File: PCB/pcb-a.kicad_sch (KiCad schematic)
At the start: 16 parts, among them Q3 BC337, Q4 BC337, SW1 config, U1 MCP23008-xP, U4 ATmega16L-8P

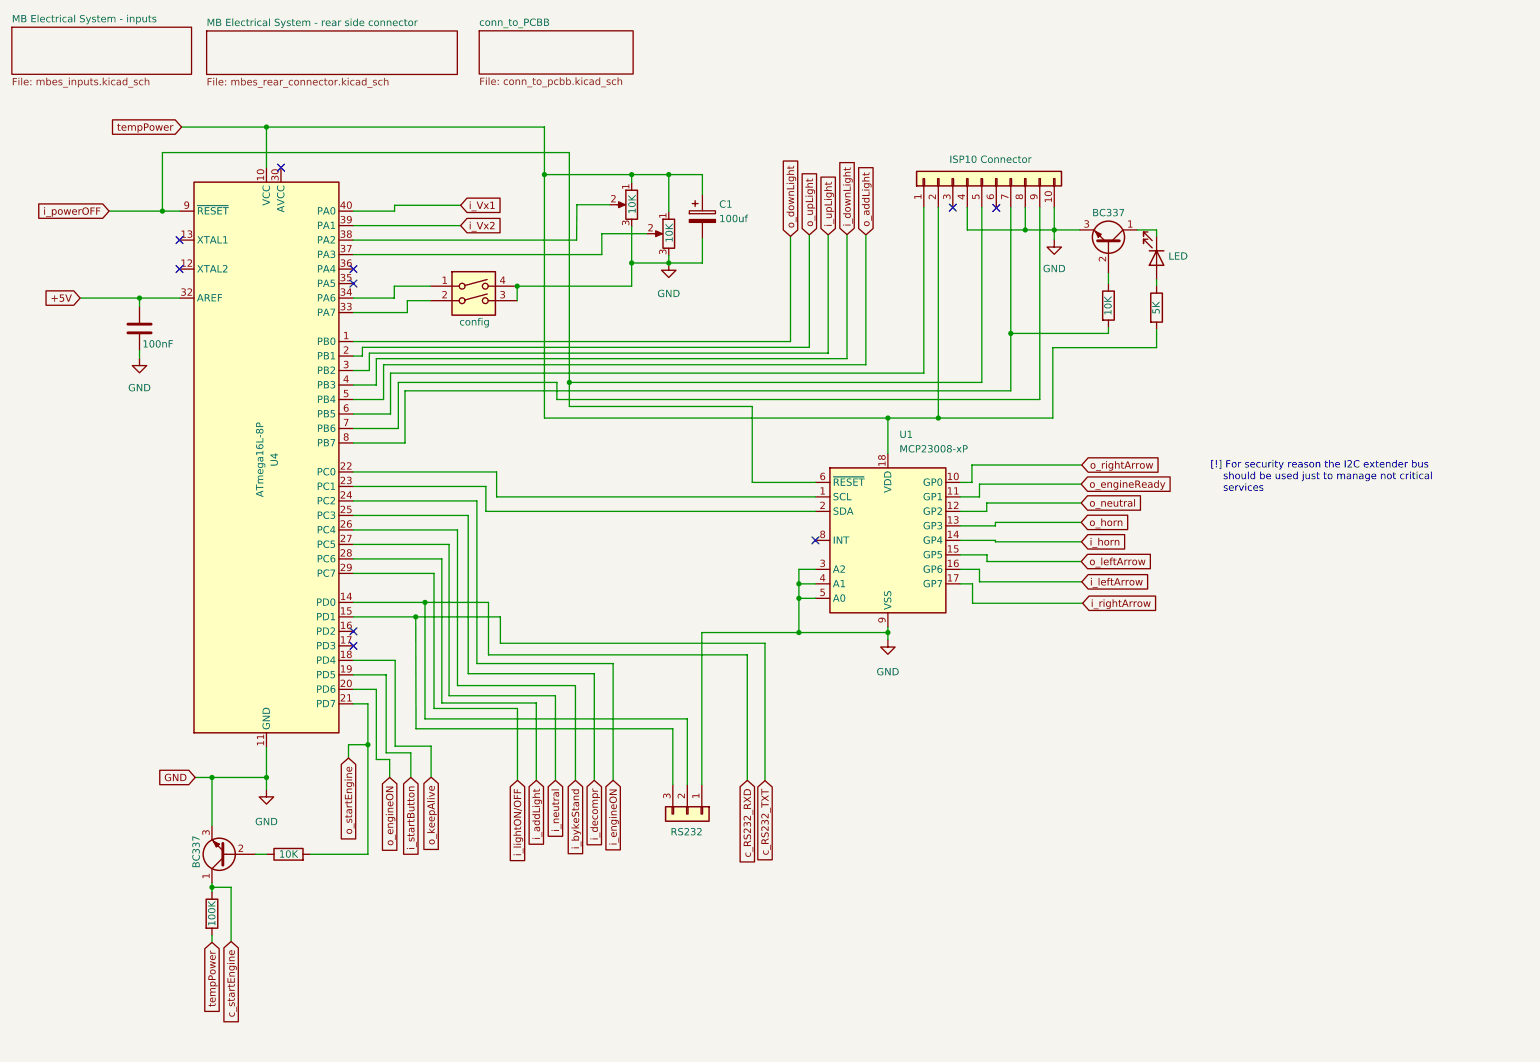
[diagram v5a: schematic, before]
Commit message: Fix: RESET pin and RS232 port fingerprint
- pull-up  resistor added to RESET pin
- RS232 port fingerprint resized to standard 4-pin port
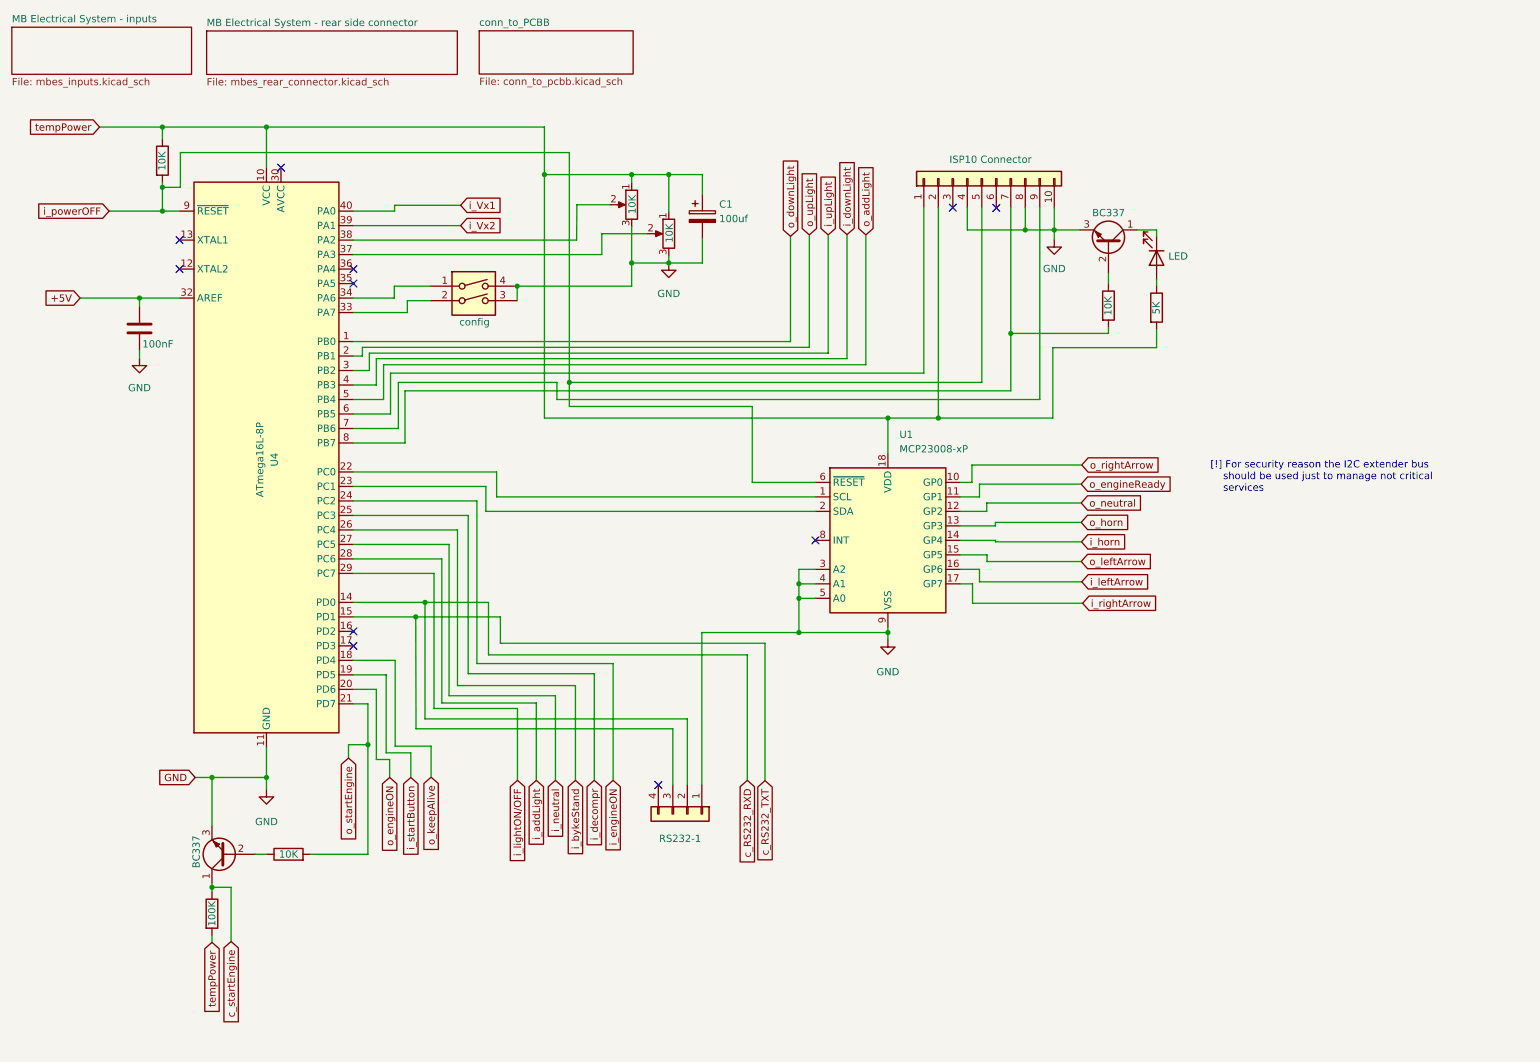
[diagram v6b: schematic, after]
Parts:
- removed RS232-1: RS232, Connector_PinSocket_2.54mm:PinSocket_1x03_P2.54mm_Vertical, symbol Connector_Generic:Conn_01x03
- added R2: 10K, Resistor_THT:R_Axial_DIN0207_L6.3mm_D2.5mm_P7.62mm_Horizontal, symbol Device:R
- added RS232-1: Conn_01x04, Connector_PinHeader_2.54mm:PinHeader_1x04_P2.54mm_Vertical, symbol Connector_Generic:Conn_01x04
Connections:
- net GND: now also RS232-1.1 (Pin_1)
- net c_RS232_RXD: now also RS232-1.2 (Pin_2)
- net c_RS232_TXT: now also RS232-1.3 (Pin_3)
- net i_powerOFF: now also R2.2
- net tempPower: now also R2.1
- no-connect marks 10 -> 11
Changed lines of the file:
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@@
   (junction (at 59.0804 149.3012) (diameter 0) (color 0 0 0 0)
   )
+  (junction (at 40.8432 35.306) (diameter 0) (color 0 0 0 0)
+  )
   (junction (at 103.0224 63.1952) (diameter 0) (color 0 0 0 0)
   )
@@
   )
   (junction (at 107.7976 43.6372) (diameter 0) (color 0 0 0 0)
+  )
+  (junction (at 40.8432 45.8724) (diameter 0) (color 0 0 0 0)
   )
   (junction (at 86.868 118.618) (diameter 0) (color 0 0 0 0)
@@
   (no_connect (at 74.3204 62.738))
   (no_connect (at 186.9948 49.4792))
+  (no_connect (at 127.762 150.622))
   (no_connect (at 61.6204 42.418))
   (no_connect (at 74.3204 60.198))
@@
     (stroke (width 0) (type default) (color 0 0 0 0))
   )
+  (wire (pts (xy 43.9928 39.7764) (xy 112.1664 39.7764))
+    (stroke (width 0) (type default) (color 0 0 0 0))
+  )
   (wire (pts (xy 123.0884 59.1312) (xy 123.0884 52.7304))
     (stroke (width 0) (type default) (color 0 0 0 0))
@@
     (stroke (width 0) (type default) (color 0 0 0 0))
   )
+  (wire (pts (xy 40.8432 45.8724) (xy 43.9928 45.8724))
+    (stroke (width 0) (type default) (color 0 0 0 0))
+  )
   (wire (pts (xy 74.3204 67.818) (xy 83.7692 67.818))
     (stroke (width 0) (type default) (color 0 0 0 0))
@@
     (stroke (width 0) (type default) (color 0 0 0 0))
   )
-  (wire (pts (xy 40.8432 39.7764) (xy 112.1664 39.7764))
-    (stroke (width 0) (type default) (color 0 0 0 0))
-  )
   (wire (pts (xy 135.4836 43.6372) (xy 129.5908 43.6372))
     (stroke (width 0) (type default) (color 0 0 0 0))
@@
     (stroke (width 0) (type default) (color 0 0 0 0))
   )
-  (wire (pts (xy 40.8432 50.038) (xy 40.8432 39.7764))
+  (wire (pts (xy 40.8432 50.038) (xy 40.8432 45.8724))
     (stroke (width 0) (type default) (color 0 0 0 0))
   )
@@
     (stroke (width 0) (type default) (color 0 0 0 0))
   )
+  (wire (pts (xy 43.9928 45.8724) (xy 43.9928 39.7764))
+    (stroke (width 0) (type default) (color 0 0 0 0))
+  )
   (wire (pts (xy 79.6036 83.058) (xy 79.6036 76.962))
     (stroke (width 0) (type default) (color 0 0 0 0))
@@
     (stroke (width 0) (type default) (color 0 0 0 0))
   )
+  (wire (pts (xy 40.8432 35.306) (xy 40.8432 37.3888))
+    (stroke (width 0) (type default) (color 0 0 0 0))
+  )
   (wire (pts (xy 74.3204 77.978) (xy 77.1144 77.978))
     (stroke (width 0) (type default) (color 0 0 0 0))
@@
     (stroke (width 0) (type default) (color 0 0 0 0))
   )
+  (wire (pts (xy 40.8432 45.8724) (xy 40.8432 45.0088))
+    (stroke (width 0) (type default) (color 0 0 0 0))
+  )
   (wire (pts (xy 185.3184 102.6668) (xy 180.6956 102.6668))
     (stroke (width 0) (type default) (color 0 0 0 0))
   )
-  (wire (pts (xy 44.196 35.306) (xy 59.0804 35.306))
+  (wire (pts (xy 29.8196 35.306) (xy 40.8432 35.306))
     (stroke (width 0) (type default) (color 0 0 0 0))
   )
@@
   )
   (wire (pts (xy 91.0844 134.9756) (xy 91.0844 108.458))
+    (stroke (width 0) (type default) (color 0 0 0 0))
+  )
+  (wire (pts (xy 40.8432 35.306) (xy 59.0804 35.306))
     (stroke (width 0) (type default) (color 0 0 0 0))
   )
@@
     )
   )
-  (global_label "tempPower" (shape input) (at 44.196 35.306 180) (fields_autoplaced)
-    (effects (font (size 1.27 1.27)) (justify right))
-    (property "Riferimenti inter-foglio" "${INTERSHEET_REFS}" (id 0) (at 31.5019 35.3854 0)
+  (global_label "tempPower" (shape input) (at 29.8196 35.306 180) (fields_autoplaced)
+    (effects (font (size 1.27 1.27)) (justify right))
+    (property "Riferimenti inter-foglio" "${INTERSHEET_REFS}" (id 0) (at 17.1255 35.3854 0)
       (effects (font (size 1.27 1.27)) (justify right) hide)
     )
@@
     (pin "9")
   )
+  (symbol (lib_id "Device:R") (at 40.8432 41.1988 0) (unit 1)
+    (in_bom yes) (on_board yes)
+    (property "Reference" "R2" (id 0) (at 46.482 41.1988 90)
+      (effects (font (size 1.27 1.27)) hide)
+    )
+    (property "Value" "10K" (id 1) (at 40.7924 41.2496 90))
+    (property "Footprint" "Resistor_THT:R_Axial_DIN0207_L6.3mm_D2.5mm_P7.62mm_Horizontal" (id 2) (at 39.0652 41.1988 90)
+      (effects (font (size 1.27 1.27)) hide)
+    )
+    (property "Datasheet" "~" (id 3) (at 40.8432 41.1988 0)
+      (effects (font (size 1.27 1.27)) hide)
+    )
+    (pin "1")
+    (pin "2")
+  )
   (symbol (lib_id "power:GND") (at 197.1548 55.0672 0) (unit 1)
     (in_bom yes) (on_board yes) (fields_autoplaced)
@@
     (pin "3")
     (pin "4")
-  )
-  (symbol (lib_id "Connector_Generic:Conn_01x03") (at 132.842 155.702 270) (unit 1)
-    (in_bom yes) (on_board yes)
-    (property "Reference" "RS232-1" (id 0) (at 128.7272 158.8516 90)
-      (effects (font (size 1.27 1.27)) (justify left) hide)
-    )
-    (property "Value" "RS232" (id 1) (at 129.8956 158.8516 90)
-      (effects (font (size 1.27 1.27)) (justify left))
-    )
-    (property "Footprint" "Connector_PinSocket_2.54mm:PinSocket_1x03_P2.54mm_Vertical" (id 2) (at 132.842 155.702 0)
-      (effects (font (size 1.27 1.27)) hide)
-    )
-    (property "Datasheet" "~" (id 3) (at 132.842 155.702 0)
-      (effects (font (size 1.27 1.27)) hide)
-    )
-    (pin "1")
-    (pin "2")
-    (pin "3")
   )
   (symbol (lib_id "Device:R") (at 206.6544 66.5988 0) (unit 1)
@@
     (pin "2")
     (pin "3")
+  )
+  (symbol (lib_id "Connector_Generic:Conn_01x04") (at 132.842 155.702 270) (unit 1)
+    (in_bom yes) (on_board yes) (fields_autoplaced)
+    (property "Reference" "RS232-1" (id 0) (at 131.572 160.02 90))
+    (property "Value" "Conn_01x04" (id 1) (at 131.572 162.56 90)
+      (effects (font (size 1.27 1.27)) hide)
+    )
+    (property "Footprint" "Connector_PinHeader_2.54mm:PinHeader_1x04_P2.54mm_Vertical" (id 2) (at 132.842 155.702 0)
+      (effects (font (size 1.27 1.27)) hide)
+    )
+    (property "Datasheet" "~" (id 3) (at 132.842 155.702 0)
+      (effects (font (size 1.27 1.27)) hide)
+    )
+    (pin "1")
+    (pin "2")
+    (pin "3")
+    (pin "4")
   )
   (symbol (lib_id "power:GND") (at 36.83 75.8444 0) (unit 1)
@@
       (reference "R1") (unit 1) (value "1K") (footprint "Resistor_THT:R_Axial_DIN0207_L6.3mm_D2.5mm_P7.62mm_Horizontal")
     )
+    (path "/720930cf-ec82-4dc2-994a-09298296c03d"
+      (reference "R2") (unit 1) (value "10K") (footprint "Resistor_THT:R_Axial_DIN0207_L6.3mm_D2.5mm_P7.62mm_Horizontal")
+    )
     (path "/b1e0026b-e442-4e9d-9275-b07005f83053"
       (reference "R6") (unit 1) (value "100K") (footprint "Resistor_THT:R_Axial_DIN0207_L6.3mm_D2.5mm_P7.62mm_Horizontal")
@@
       (reference "R9") (unit 1) (value "5K") (footprint "Resistor_THT:R_Axial_DIN0207_L6.3mm_D2.5mm_P7.62mm_Horizontal")
     )
-    (path "/9642f9cf-4b46-422a-a864-ecd9c3909353"
-      (reference "RS232-1") (unit 1) (value "RS232") (footprint "Connector_PinSocket_2.54mm:PinSocket_1x03_P2.54mm_Vertical")
+    (path "/c9774949-c461-4c76-91ad-3c30a5da3235"
+      (reference "RS232-1") (unit 1) (value "Conn_01x04") (footprint "Connector_PinHeader_2.54mm:PinHeader_1x04_P2.54mm_Vertical")
     )
     (path "/dfeffa1f-9119-4780-8aed-ab76c9242c17"

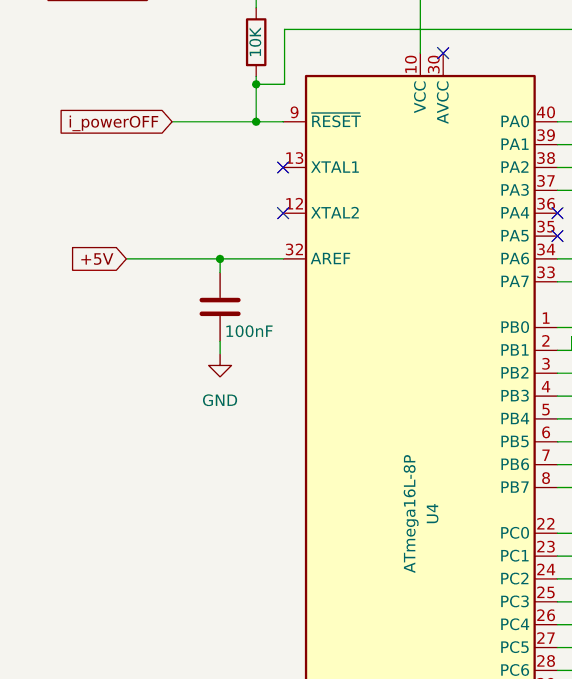
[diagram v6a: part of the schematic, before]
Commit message: External oscillator
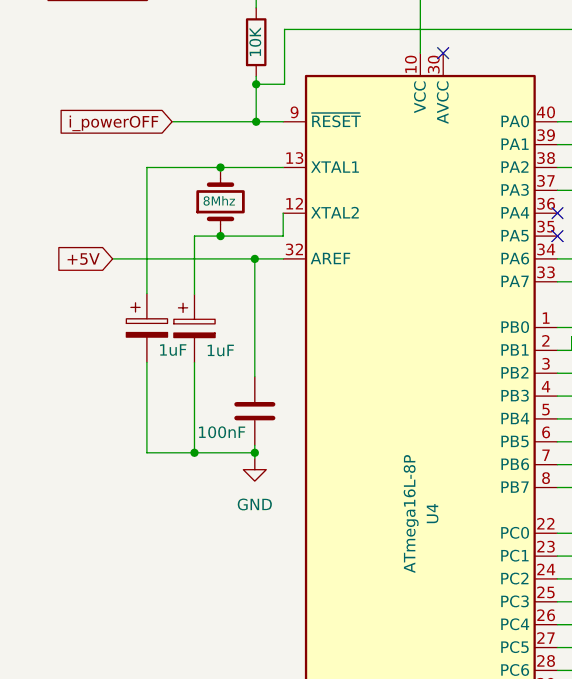
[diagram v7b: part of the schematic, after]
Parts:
- added C3, C4: 1uF, Capacitor_THT:CP_Radial_D6.3mm_P2.50mm, symbol Device:C_Polarized
- added Y1: 8Mhz, Crystal:Crystal_HC49-U_Vertical, symbol Device:Crystal
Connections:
- net GND: now also C3.2, C4.2
- net at U4.12 (XTAL2): now also C4.1, Y1.1
- net at U4.13 (XTAL1): now also C3.1, Y1.2
- no-connect marks 11 -> 9

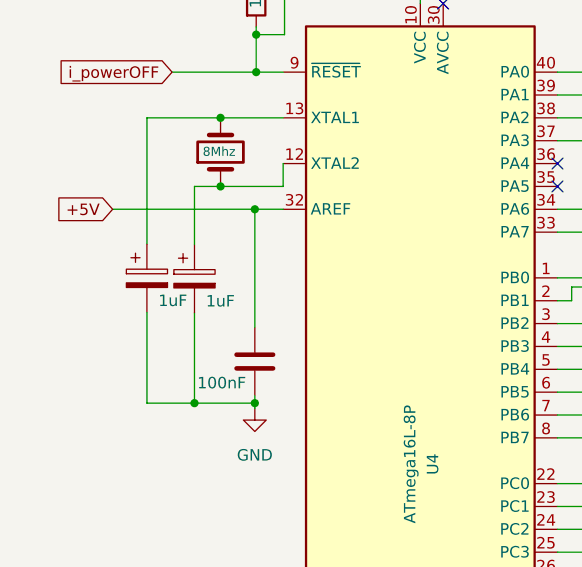
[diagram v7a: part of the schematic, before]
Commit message: Wrong capacitors type fixed
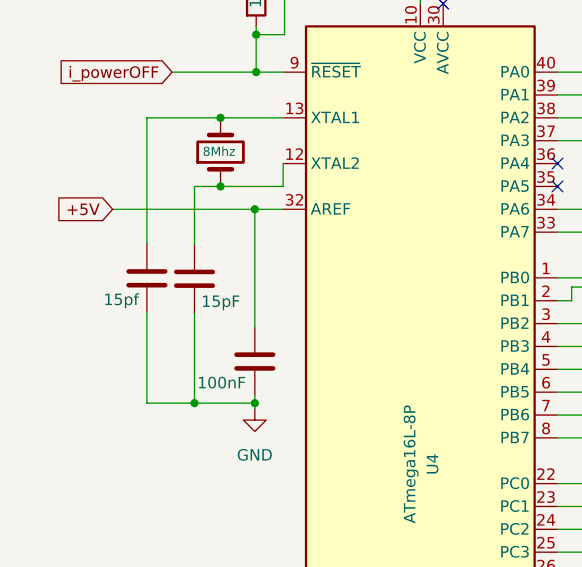
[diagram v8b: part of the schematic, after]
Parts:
- removed C3, C4: 1uF, Capacitor_THT:CP_Radial_D6.3mm_P2.50mm, symbol Device:C_Polarized
- added C3: 15pf, Capacitor_THT:C_Disc_D6.0mm_W2.5mm_P5.00mm, symbol Device:C
- added C4: 15pF, Capacitor_THT:C_Disc_D6.0mm_W2.5mm_P5.00mm, symbol Device:C
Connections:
- net GND: now also C3.2, C4.2
- net at U4.13 (XTAL1), Y1.2: now also C3.1
- net at U4.12 (XTAL2), Y1.1: now also C4.1
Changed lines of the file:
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@@
-    (pin "2")
-  )
-  (symbol (lib_id "Device:C_Polarized") (at 28.702 72.9488 0) (unit 1)
-    (in_bom yes) (on_board yes)
-    (property "Reference" "C3" (id 0) (at 32.1564 70.7897 0)
-      (effects (font (size 1.27 1.27)) (justify left) hide)
-    )
-    (property "Value" "1uF" (id 1) (at 29.972 75.438 0)
-      (effects (font (size 1.27 1.27)) (justify left))
-    )
-    (property "Footprint" "Capacitor_THT:CP_Radial_D6.3mm_P2.50mm" (id 2) (at 29.6672 76.7588 0)
-      (effects (font (size 1.27 1.27)) hide)
-    )
-    (property "Datasheet" "~" (id 3) (at 28.702 72.9488 0)
-      (effects (font (size 1.27 1.27)) hide)
-    )
-    (pin "1")
     (pin "2")
   )
@@
     (pin "2")
   )
+  (symbol (lib_id "Device:C") (at 33.9852 72.9996 0) (unit 1)
+    (in_bom yes) (on_board yes)
+    (property "Reference" "C4" (id 0) (at 37.0332 71.7295 0)
+      (effects (font (size 1.27 1.27)) (justify left) hide)
+    )
+    (property "Value" "15pF" (id 1) (at 34.7472 75.5396 0)
+      (effects (font (size 1.27 1.27)) (justify left))
+    )
+    (property "Footprint" "Capacitor_THT:C_Disc_D6.0mm_W2.5mm_P5.00mm" (id 2) (at 34.9504 76.8096 0)
+      (effects (font (size 1.27 1.27)) hide)
+    )
+    (property "Datasheet" "~" (id 3) (at 33.9852 72.9996 0)
+      (effects (font (size 1.27 1.27)) hide)
+    )
+    (pin "1")
+    (pin "2")
+  )
   (symbol (lib_id "Connector_Generic:Conn_01x10") (at 184.4548 44.3484 90) (unit 1)
     (in_bom yes) (on_board yes)
@@
     )
     (pin "1")
+  )
+  (symbol (lib_id "Device:C") (at 28.702 72.9488 0) (unit 1)
+    (in_bom yes) (on_board yes)
+    (property "Reference" "C3" (id 0) (at 31.75 71.6787 0)
+      (effects (font (size 1.27 1.27)) (justify left) hide)
+    )
+    (property "Value" "15pf" (id 1) (at 23.876 75.3364 0)
+      (effects (font (size 1.27 1.27)) (justify left))
+    )
+    (property "Footprint" "Capacitor_THT:C_Disc_D6.0mm_W2.5mm_P5.00mm" (id 2) (at 29.6672 76.7588 0)
+      (effects (font (size 1.27 1.27)) hide)
+    )
+    (property "Datasheet" "~" (id 3) (at 28.702 72.9488 0)
+      (effects (font (size 1.27 1.27)) hide)
+    )
+    (pin "1")
+    (pin "2")
   )
   (symbol (lib_id "Interface_Expansion:MCP23008-xP") (at 167.9956 107.7468 0) (unit 1)
@@
     (pin "1")
   )
-  (symbol (lib_id "Device:C_Polarized") (at 33.9852 72.9996 0) (unit 1)
-    (in_bom yes) (on_board yes)
-    (property "Reference" "C4" (id 0) (at 37.4396 70.8405 0)
-      (effects (font (size 1.27 1.27)) (justify left) hide)
-    )
-    (property "Value" "1uF" (id 1) (at 35.2552 75.4888 0)
-      (effects (font (size 1.27 1.27)) (justify left))
-    )
-    (property "Footprint" "Capacitor_THT:CP_Radial_D6.3mm_P2.50mm" (id 2) (at 34.9504 76.8096 0)
-      (effects (font (size 1.27 1.27)) hide)
-    )
-    (property "Datasheet" "~" (id 3) (at 33.9852 72.9996 0)
-      (effects (font (size 1.27 1.27)) hide)
-    )
-    (pin "1")
-    (pin "2")
-  )
   (symbol (lib_id "power:GND") (at 167.9956 125.1712 0) (unit 1)
     (in_bom yes) (on_board yes) (fields_autoplaced)
@@
       (reference "C2") (unit 1) (value "100nF") (footprint "Capacitor_THT:C_Disc_D6.0mm_W2.5mm_P5.00mm")
     )
-    (path "/34f57820-c171-44c5-9f63-c014c6111fed"
-      (reference "C3") (unit 1) (value "1uF") (footprint "Capacitor_THT:CP_Radial_D6.3mm_P2.50mm")
-    )
-    (path "/d6ff9b8c-3732-40ca-a91b-cd8dd554c9a3"
-      (reference "C4") (unit 1) (value "1uF") (footprint "Capacitor_THT:CP_Radial_D6.3mm_P2.50mm")
+    (path "/5db210ab-3365-4585-8c98-d88f4ce697bb"
+      (reference "C3") (unit 1) (value "15pf") (footprint "Capacitor_THT:C_Disc_D6.0mm_W2.5mm_P5.00mm")
+    )
+    (path "/4e6a43d5-5571-49b3-bd07-86f7e9615a31"
+      (reference "C4") (unit 1) (value "15pF") (footprint "Capacitor_THT:C_Disc_D6.0mm_W2.5mm_P5.00mm")
     )
     (path "/019cc045-c77b-4d0b-997a-4367367b2f1b"
